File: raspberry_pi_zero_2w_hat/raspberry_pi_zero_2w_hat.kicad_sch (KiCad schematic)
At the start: 18 parts, among them J1 GPIO, SW1 SW_DIP_x04, SW2 SW_Nidec_CAS-120A1, U1 CAT24C256, U3 NRF24L01P

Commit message: Added transmission LED to schematics
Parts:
- added D5: LED, symbol Device:LED
- added R7: 220, Resistor_THT:R_Axial_DIN0516_L15.5mm_D5.0mm_P20.32mm_Horizontal, symbol Device:R_US
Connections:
- net GND: now also D5.1 (K)
- net GPIO21/PCM.DOUT: now also R7.1
- new net: D5.2 (A), R7.2
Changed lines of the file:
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@@
+	(wire
+		(pts
+			(xy 185.42 86.36) (xy 189.23 86.36)
+		)
+		(stroke
+			(width 0)
+			(type default)
+		)
+	)
 	(wire
 		(pts
@@
 	(wire
 		(pts
+			(xy 189.23 86.36) (xy 189.23 87.63)
+		)
+		(stroke
+			(width 0)
+			(type default)
+		)
+	)
+	(wire
+		(pts
 			(xy 135.89 45.72) (xy 162.56 45.72)
 		)
@@
 	(wire
 		(pts
-			(xy 135.89 86.36) (xy 162.56 86.36)
+			(xy 135.89 86.36) (xy 166.37 86.36)
 		)
 		(stroke
@@
 		(pts
 			(xy 187.96 50.8) (xy 191.77 50.8)
+		)
+		(stroke
+			(width 0)
+			(type default)
+		)
+	)
+	(wire
+		(pts
+			(xy 173.99 86.36) (xy 177.8 86.36)
 		)
 		(stroke
@@
 	)
 	(symbol
+		(lib_id "Device:R_US")
+		(at 170.18 86.36 90)
+		(unit 1)
+		(exclude_from_sim no)
+		(in_bom yes)
+		(on_board yes)
+		(dnp no)
+		(property "Reference" "R7"
+			(at 166.878 85.09 90)
+			(effects
+				(font
+					(size 1.27 1.27)
+				)
+			)
+		)
+		(property "Value" "220"
+			(at 173.99 85.09 90)
+			(effects
+				(font
+					(size 1.27 1.27)
+				)
+			)
+		)
+		(property "Footprint" "Resistor_THT:R_Axial_DIN0516_L15.5mm_D5.0mm_P20.32mm_Horizontal"
+			(at 170.434 85.344 90)
+			(effects
+				(font
+					(size 1.27 1.27)
+				)
+				(hide yes)
+			)
+		)
+		(property "Datasheet" "~"
+			(at 170.18 86.36 0)
+			(effects
+				(font
+					(size 1.27 1.27)
+				)
+				(hide yes)
+			)
+		)
+		(property "Description" "Resistor, US symbol"
+			(at 170.18 86.36 0)
+			(effects
+				(font
+					(size 1.27 1.27)
+				)
+				(hide yes)
+			)
+		)
+		(pin "2"
+		)
+		(pin "1"
+		)
+		(instances
+			(project "raspberry_pi_zero_2w_hat"
+				(path "/e63e39d7-6ac0-4ffd-8aa3-1841a4541b55"
+					(reference "R7")
+					(unit 1)
+				)
+			)
+		)
+	)
+	(symbol
 		(lib_id "Device:C_Small")
 		(at 67.31 177.8 0)
@@
 	)
 	(symbol
+		(lib_id "Device:LED")
+		(at 181.61 86.36 180)
+		(unit 1)
+		(exclude_from_sim no)
+		(in_bom yes)
+		(on_board yes)
+		(dnp no)
+		(property "Reference" "D5"
+			(at 179.07 85.598 0)
+			(effects
+				(font
+					(size 1.27 1.27)
+				)
+			)
+		)
+		(property "Value" "LED"
+			(at 181.864 84.074 0)
+			(effects
+				(font
+					(size 1.27 1.27)
+				)
+				(hide yes)
+			)
+		)
+		(property "Footprint" ""
+			(at 181.61 86.36 0)
+			(effects
+				(font
+					(size 1.27 1.27)
+				)
+				(hide yes)
+			)
+		)
+		(property "Datasheet" "~"
+			(at 181.61 86.36 0)
+			(effects
+				(font
+					(size 1.27 1.27)
+				)
+				(hide yes)
+			)
+		)
+		(property "Description" "Light emitting diode"
+			(at 181.61 86.36 0)
+			(effects
+				(font
+					(size 1.27 1.27)
+				)
+				(hide yes)
+			)
+		)
+		(pin "2"
+		)
+		(pin "1"
+		)
+		(instances
+			(project "raspberry_pi_zero_2w_hat"
+				(path "/e63e39d7-6ac0-4ffd-8aa3-1841a4541b55"
+					(reference "D5")
+					(unit 1)
+				)
+			)
+		)
+	)
+	(symbol
 		(lib_id "Jumper:SolderJumper_2_Open")
 		(at 96.52 180.34 0)
@@
 					(unit 1)
 				)
+			)
+		)
+	)
+	(symbol
+		(lib_name "GND_1")
+		(lib_id "power:GND")
+		(at 189.23 87.63 0)
+		(unit 1)
+		(exclude_from_sim no)
+		(in_bom yes)
+		(on_board yes)
+		(dnp no)
+		(fields_autoplaced yes)
+		(property "Reference" "#PWR012"
+			(at 189.23 93.98 0)
+			(effects
+				(font
+					(size 1.27 1.27)
+				)
+				(hide yes)
+			)
+		)
+		(property "Value" "GND"
+			(at 189.23 92.71 0)
+			(effects
+				(font
+					(size 1.27 1.27)
+				)
+			)
+		)
+		(property "Footprint" ""
+			(at 189.23 87.63 0)
+			(effects
+				(font
+					(size 1.27 1.27)
+				)
+				(hide yes)
+			)
+		)
+		(property "Datasheet" ""
+			(at 189.23 87.63 0)
+			(effects
+				(font
+					(size 1.27 1.27)
+				)
+				(hide yes)
+			)
+		)
+		(property "Description" "Power symbol creates a global label with name \"GND\" , ground"
+			(at 189.23 87.63 0)
+			(effects
+				(font
+					(size 1.27 1.27)
+				)
+				(hide yes)
+			)
+		)
+		(pin "1"
+		)
+		(instances
+			(project "raspberry_pi_zero_2w_hat"
+				(path "/e63e39d7-6ac0-4ffd-8aa3-1841a4541b55"
+					(reference "#PWR012")
+					(unit 1)
+				)

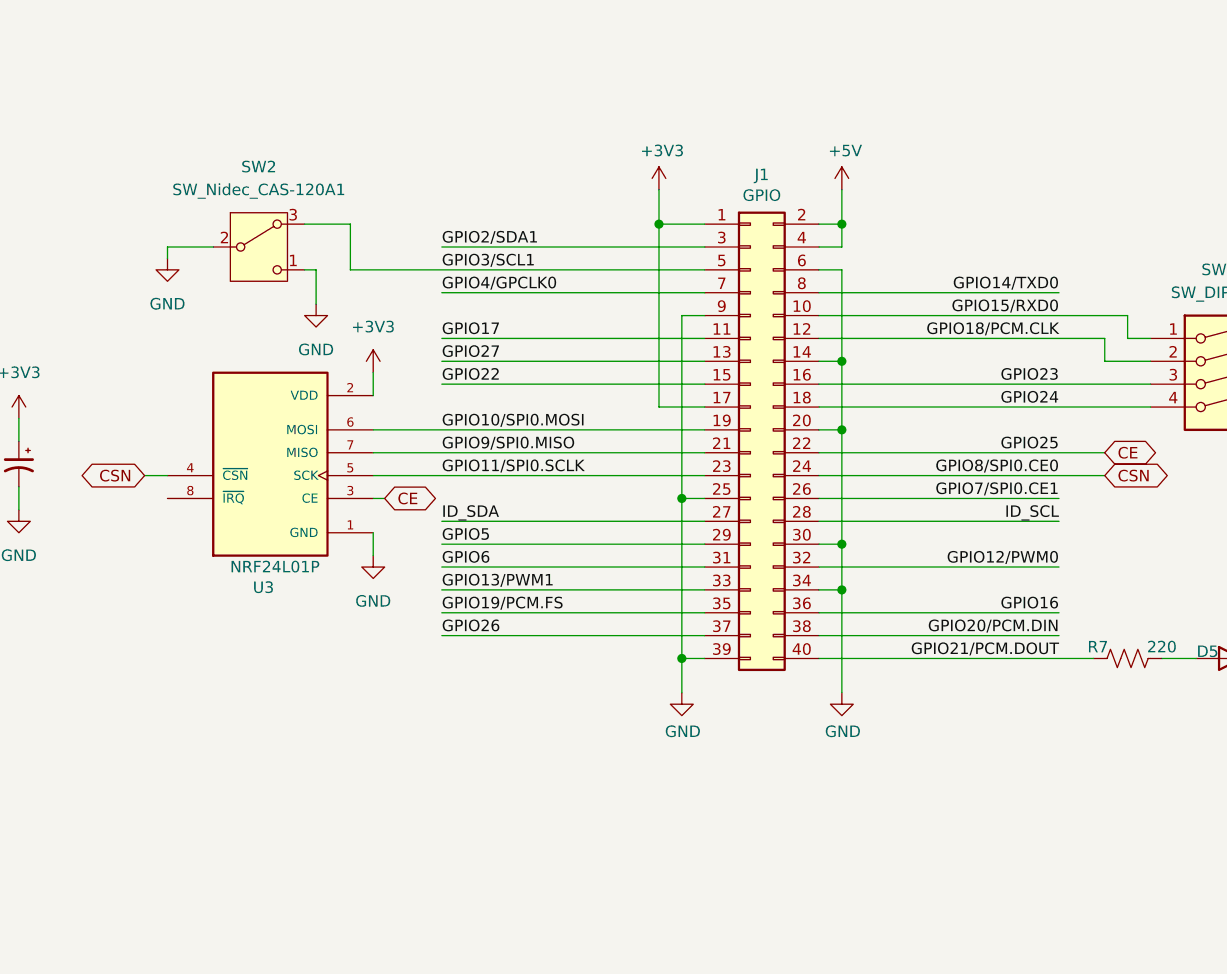
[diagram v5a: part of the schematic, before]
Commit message: ERC errors solved
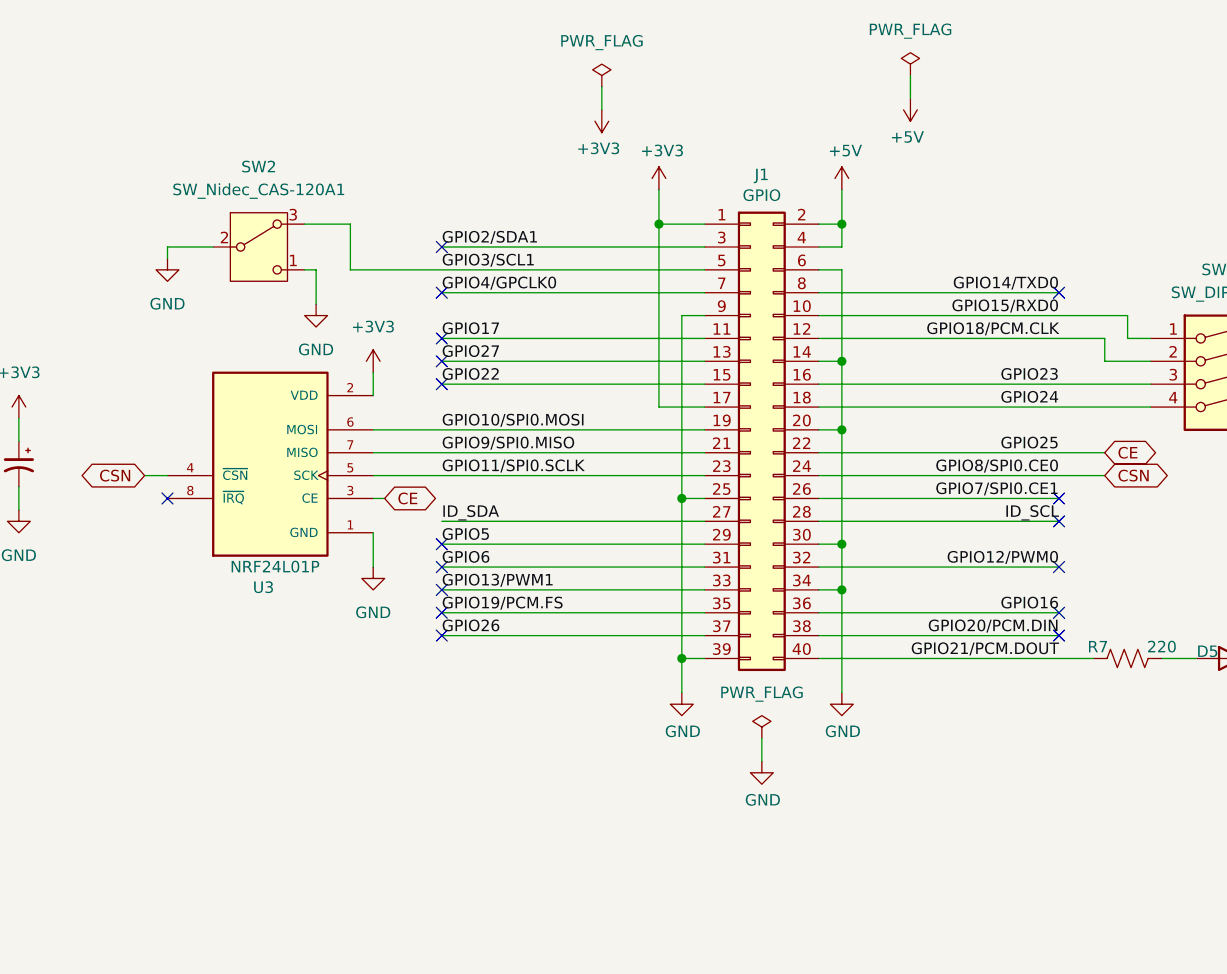
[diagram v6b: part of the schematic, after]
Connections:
- no-connect marks 3 -> 20
